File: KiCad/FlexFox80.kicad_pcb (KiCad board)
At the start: 4 copper layers, 111.2 x 80 mm, 315 parts, among them J101 Jumper_NO_Small, J102 Jumper_NO_Small, J203 V4, J307 Jumper_NC_Small, J501 GND, J502 DET, J503 DET, J504 GND, J505 DET, J506 GND, J507 DET, J508 GND, P101 Phoenix, P103 Phoenix, P202 To Power Supply Board, P203 AUX BATTERY, P301 ISP/PDI, P302 Thru, P303 Header, P304 Header, Q101 LMN400E01, Q102 IRF610, Q103 AFT05MS004N, U101 DAC081C085, U102 OPA171, U104 THS9001, U105 MIC5219-5.0YM5, U107 LM5134B, U110 MIC5219-3.3BM5, U201 DAC081C085, U202 OPA171, U203 LTC3600, U301 DS3231, U302 TS5A3157, U303 ATMEGA328P, U304 SI5351A, U305 74HC1G08, U306 MIC5219-3.3BM5, U307 SN74CB3Q3305, U308 MIC5219-3.3BM5, X301 ASTX-H11-25.MHZ

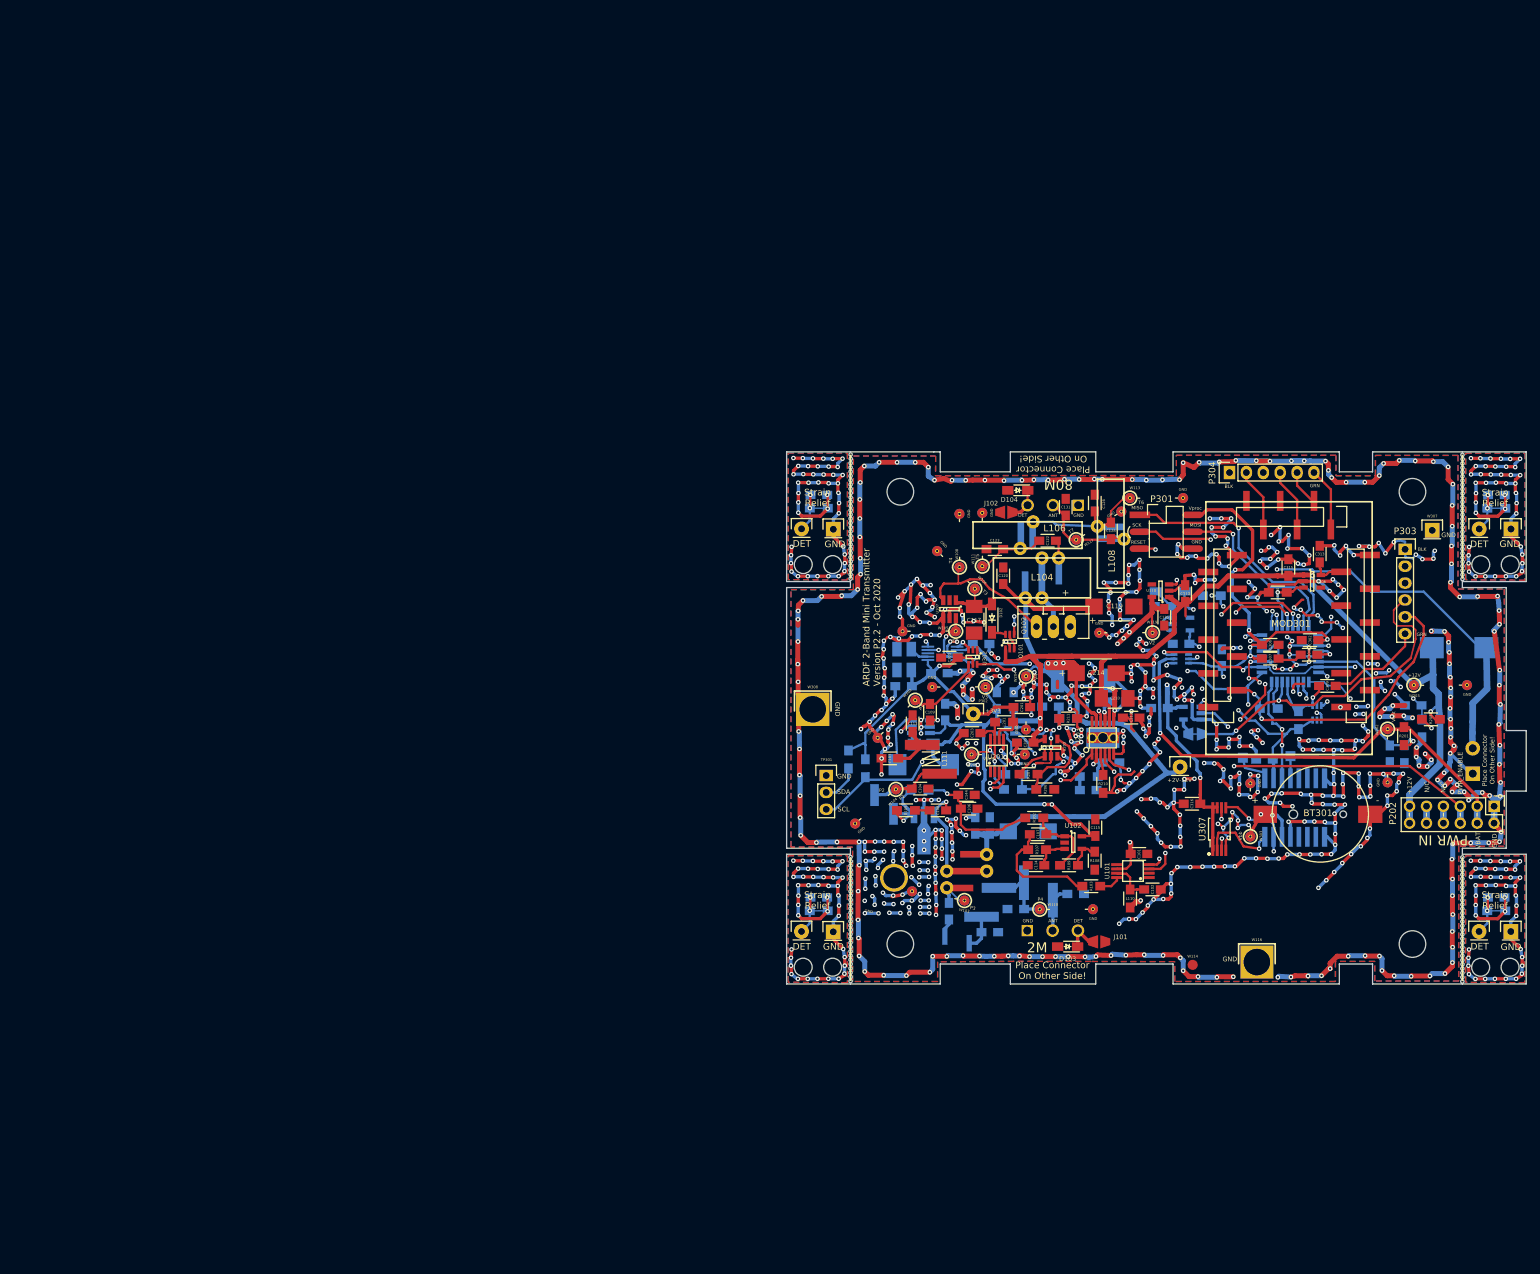
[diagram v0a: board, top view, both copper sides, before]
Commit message: PCB Updates
o Started PCB layout
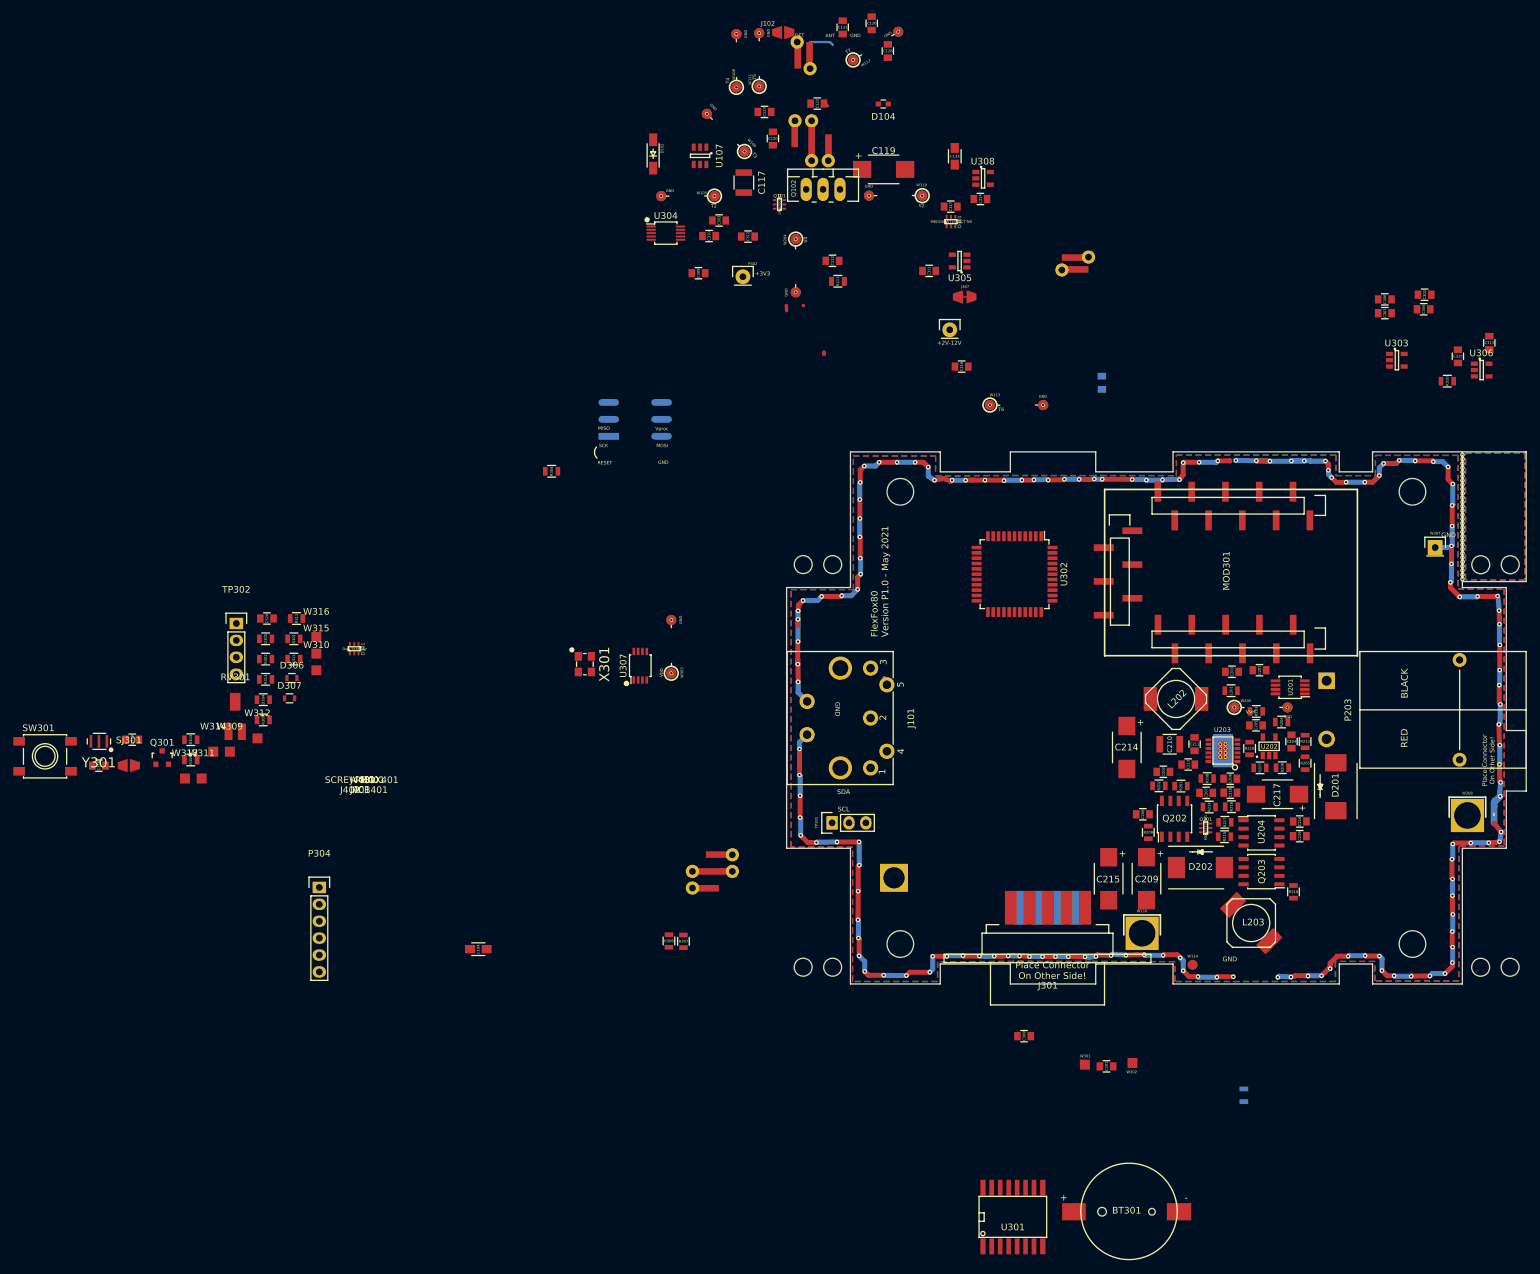
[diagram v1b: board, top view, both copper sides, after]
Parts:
- removed the ? at (117.8, 98.1)
- removed the ? at (117.8, 97.4)
- removed the ? at (117.8, 104.5)
- removed the ? at (117.8, 103.8)
- removed the ? at (117.8, 103.2)
- removed the ? at (117.8, 102.5)
- removed the ? at (117.8, 101.9)
- removed the ? at (117.8, 101.3)
- removed the ? at (117.8, 100.6)
- removed the ? at (117.8, 100.0)
- removed the ? at (117.8, 105.1)
- removed the ? at (117.8, 105.8)
- removed the ? at (117.8, 106.4)
- removed the ? at (117.8, 107.0)
- removed the ? at (117.8, 107.7)
- removed the ? at (117.8, 108.3)
- removed the ? at (117.8, 109.0)
- removed the ? at (117.8, 109.6)
- removed the ? at (117.8, 91.6)
- removed the ? at (117.8, 92.3)
- removed the ? at (117.8, 92.9)
- removed the ? at (117.8, 93.5)
- removed the ? at (117.8, 94.2)
- removed the ? at (117.8, 94.8)
- removed the ? at (117.8, 95.5)
- removed the ? at (117.8, 96.1)
- removed the ? at (117.8, 96.8)
- removed the ? at (117.8, 91.0)
- removed the ? at (25.8, 38.8)
- removed the ? at (25.8, 38.1)
- removed the ? at (25.8, 37.5)
- removed the ? at (25.8, 36.8)
- removed the ? at (25.8, 36.2)
- removed the ? at (25.8, 35.5)
- removed the ? at (25.8, 34.9)
- removed the ? at (25.8, 34.3)
- removed the ? at (25.8, 30.4)
- removed the ? at (25.8, 31.0)
- removed the ? at (25.8, 31.7)
- removed the ? at (25.8, 32.3)
- removed the ? at (25.8, 33.0)
- removed the ? at (25.8, 33.6)
- removed the ? at (25.8, 43.9)
- removed the ? at (25.8, 43.3)
- removed the ? at (25.8, 42.6)
- removed the ? at (25.8, 42.0)
- removed the ? at (25.8, 41.3)
- removed the ? at (25.8, 40.7)
- removed the ? at (25.8, 40.0)
- removed the ? at (25.8, 39.4)
- removed the ? at (25.8, 44.6)
- removed the ? at (25.8, 45.2)
- removed the ? at (25.8, 45.8)
- removed the ? at (25.8, 46.5)
- removed the ? at (25.8, 47.1)
- removed the ? at (25.8, 47.8)
- removed the ? at (25.8, 48.4)
- removed the ? at (25.8, 49.1)
- removed the ? at (25.8, 109.6)
- removed the ? at (25.8, 109.0)
- removed the ? at (25.8, 108.3)
- removed the ? at (25.8, 107.7)
- removed the ? at (25.8, 107.0)
- removed the ? at (25.8, 106.4)
- removed the ? at (25.8, 105.7)
- removed the ? at (25.8, 105.1)
- removed the ? at (25.8, 99.9)
- removed the ? at (25.8, 100.6)
- removed the ? at (25.8, 101.2)
- removed the ? at (25.8, 101.9)
- removed the ? at (25.8, 102.5)
- removed the ? at (25.8, 103.2)
- removed the ? at (25.8, 103.8)
- removed the ? at (25.8, 104.4)
- removed the ? at (25.8, 94.2)
- removed the ? at (25.8, 93.5)
- removed the ? at (25.8, 92.9)
- removed the ? at (25.8, 92.2)
- removed the ? at (25.8, 91.6)
- removed the ? at (25.8, 90.9)
- removed the ? at (25.8, 94.8)
- removed the ? at (25.8, 95.4)
- removed the ? at (25.8, 96.1)
- removed the ? at (25.8, 96.7)
- removed the ? at (25.8, 97.4)
- removed the ? at (25.8, 98.0)
- removed the ? at (25.8, 98.7)
- removed the ? at (25.8, 99.3)
- removed the ? at (117.8, 99.3)
- removed the ? at (117.8, 98.7)
- removed C101, C102: 10uF, Capacitors_SMD:C_0805_HandSoldering
- removed C103, C130: 20pF, Capacitors_SMD:C_0805_HandSoldering
- removed C105, C118: 100nF, Capacitors_SMD:C_0805_HandSoldering
- removed C106, C110: 10nF, Capacitors_SMD:C_0805_HandSoldering
- removed C107: 22nF, Capacitors_SMD:C_0805_HandSoldering
- removed C108, C109, C111, C113, C144: 1nF, Capacitors_SMD:C_0805_HandSoldering
- removed C112: 33pF, Capacitors_SMD:C_0805_HandSoldering
- removed C114: 33nF, Capacitors_SMD:C_0805_HandSoldering
- removed C115: 1uF, Capacitors_SMD:C_0805_HandSoldering
- removed C121: 100pF, Capacitors_SMD:C_0805_HandSoldering
- removed C125: 47uF low ESR, Capacitors_SMD:C_2917_7343_Metric_HandSoldering
- removed C132, C135, C141: 2.2uF, Capacitors_SMD:C_0805_HandSoldering
- removed C501, C502, C503, C504: np, Capacitors_SMD:C_0805_HandSoldering
- removed D103: 5V, Diodes_SMD:SOD-323F_Handsolder
- removed D302: 4.7V, Diodes_SMD:SOD-123_Handsolder
- removed D303: MBD54DWT1G_Schottky_Ind, TO_SOT_Packages_SMD:SOT-363_Handsolder
- removed J501, J504, J506, J508: GND, Pin_Headers:Pin_Header_Straight_1x01
- removed J502, J503, J505, J507: DET, Pin_Headers:Pin_Header_Straight_1x01_circle_pad
- removed L101: 82nH, Inductors:Wurth_744912212
- removed L102: 470nH, Inductors:L_0805_2015_Handsolder
- removed L105: 120nH, Inductors:Wurth_744912212
- removed L107: 8nH, Inductors:Wurth_744913080
- removed L109: 13nH, Inductors:Wurth_744911112
- removed L110: 10uH, Resistors_SMD:R_0805_HandSoldering
- removed L111: 56nH, Inductors:Wurth_744912212
- removed P101, P103: Phoenix, Sockets:Phoenix_3.81mm_3pos
- removed P202: To Power Supply Board, Pin_Headers:Pin_Header_Straight_2x06
- removed P303: Header, Pin_Headers:Pin_Header_Straight_1x06
- removed Q103: AFT05MS004N, TO_SOT_Packages_SMD:SOT89-3_Housing_Handsoldering
- removed R101: 49.9k, Resistors_SMD:R_0805_HandSoldering
- removed R102: 10, Resistors_SMD:R_0805_HandSoldering
- removed R103: 16k, Resistors_SMD:R_0805_HandSoldering
- removed R104: 51, Resistors_SMD:R_0805_HandSoldering
- removed R105: 270, Resistors_SMD:R_0805_HandSoldering
- removed R106: 240 2W, Resistors_SMD:R_2512_HandSoldering
- removed R107: 11k, Resistors_SMD:R_0805_HandSoldering
- removed R108: 15k, Resistors_SMD:R_0805_HandSoldering
- removed R109: 7.5k, Resistors_SMD:R_0805_HandSoldering
- removed R501, R502, R503, R504: 0, Resistors_SMD:Zero_Ohm_0805_HandSoldering
- removed U101: DAC081C085, SMD_Packages:SSOP-8_Handsolder
- removed U102: OPA171, TO_SOT_Packages_SMD:SOT-23-5_Handsolder
- removed U104: THS9001, TO_SOT_Packages_SMD:SOT-23-6_Handsolder
- removed U105: MIC5219-5.0YM5, TO_SOT_Packages_SMD:SOT-23-5_Handsolder
- removed U110: MIC5219-3.3BM5, TO_SOT_Packages_SMD:SOT-23-5_Handsolder
- removed W101: V3, Measurement_Points:Measurement_Point_ScopeProbe_Round-SMD-2sides-Pad_Small
- removed W102: P1, Measurement_Points:Measurement_Point_ScopeProbe_Round-SMD-2sides-Pad_Small
- removed W103: P3, Measurement_Points:Measurement_Point_ScopeProbe_Round-SMD-2sides-Pad_Small
- removed W104: P2, Measurement_Points:Measurement_Point_ScopeProbe_Round-SMD-2sides-Pad_Small
- removed W110: P4, Measurement_Points:Measurement_Point_ScopeProbe_Round-SMD-2sides-Pad_Small
- removed W202: Vbat, Measurement_Points:Measurement_Point_ScopeProbe_Round-SMD-2sides-Pad_Small
- removed W203: +12V, Measurement_Points:Measurement_Point_ScopeProbe_Round-SMD-2sides-Pad_Small
- added BOX401: Chassis Box, Oddities:Dummy_Empty, F.Cu at (-45.0, 81.8)
- added C206: 100nF, Capacitors_SMD:C_0805, F.Cu at (69.8, 84.5)
- added C209: 150uF low ESR, Capacitors_SMD:C_2917, F.Cu at (70.3, 94.2)
- added C215: 150uF low ESR, Capacitors_SMD:C_2917, F.Cu at (64.6, 94.2)
- added C216: 10uF, Capacitors_SMD:C_0805, F.Cu at (93.4, 85.6)
- added C217: 47uF low ESR, Capacitors_SMD:C_2917, F.Cu at (90.0, 81.5)
- added C218: 10nF, Capacitors_SMD:C_0805, F.Cu at (82.9, 81.2)
- added C219: 1uF, Capacitors_SMD:C_0805, F.Cu at (93.3, 87.8)
- added C318: 4.7uF, Capacitors_SMD:C_0805, F.Cu at (-87.2, 77.2)
- added C319: 100nF, Capacitors_SMD:C_0805, F.Cu at (-82.2, 73.3)
- added C320: 100nF, Capacitors_SMD:C_0805, F.Cu at (-61.9, 55.1)
- added D101: Dual Schottky, TO_SOT_Packages_SMD:SOT-363-0.65, F.Cu at (-48.8, 59.6)
- added D202: B530, Diodes_SMD:DO-214AB, F.Cu at (78.4, 92.5)
- added D304: GREEN, Resistors_SMD:R_0805, F.Cu at (-62.5, 67.3)
- added D305: RED, Resistors_SMD:R_0805, F.Cu at (-62.1, 58.1)
- added D306: ESD, Resistors_SMD:R_0603, F.Cu at (-58.2, 64.0)
- added D307: ESD, Resistors_SMD:R_0603, F.Cu at (-58.5, 67.1)
- added J301: DB9_Female, Connect:DB9F_CI, F.Cu at (55.5, 101.1)
- added J401: CONN_01X06, Oddities:Dummy_Empty, F.Cu at (-48.0, 83.3)
- added J402: CONN_01X10, Oddities:Dummy_Empty, F.Cu at (-49.5, 83.3)
- added J403: CONN_01X10, Oddities:Dummy_Empty, F.Cu at (-48.0, 81.8)
- added L203: 6.8uH, Inductors:CDR7D28MN, F.Cu at (86.0, 100.8)
- added PCB401: Circuit Board, Oddities:Dummy_Empty, F.Cu at (-46.5, 83.3)
- added PH401: Power Pole Staple, Oddities:Dummy_Empty, F.Cu at (-46.5, 81.8)
- added Q201: MUN5213DW1, TO_SOT_Packages_SMD:SOT-363-0.65, F.Cu at (79.2, 86.5)
- added Q202: DMP4025LSD, Housings_SOIC:SOIC-8_3.9x4.9mm_Pitch1.27mm, F.Cu at (74.5, 85.2)
- added Q203: RJK0354DSP, Housings_SOIC:SOIC-8_3.9x4.9mm_Pitch1.27mm, F.Cu at (87.6, 93.1)
- added Q301: PN2222A, TO_SOT_Packages_SMD:SOT-23, F.Cu at (-77.7, 76.0)
- added R209: 100k, Resistors_SMD:R_0805, F.Cu at (70.6, 87.2)
- added R214: 10k, Resistors_SMD:R_0805, F.Cu at (79.8, 83.4)
- added R215: 10k, Resistors_SMD:R_0805, F.Cu at (82.0, 87.9)
- added R216: 10k, Resistors_SMD:R_0805, F.Cu at (83.1, 83.3)
- added R217: 1.1k, Resistors_SMD:R_0805, F.Cu at (82.1, 85.7)
- added R218: 0.01 0.5W, Resistors_SMD:R_0805, F.Cu at (92.4, 96.2)
- added R301: 470, Resistors_SMD:R_0805, F.Cu at (-57.9, 58.1)
- added R302: 470, Resistors_SMD:R_0805, F.Cu at (-62.1, 61.2)
- added R303: 10k, Resistors_SMD:R_0805, F.Cu at (-73.4, 73.3)
- added R308: 100k, Resistors_SMD:R_0805, F.Cu at (-62.5, 70.3)
- added R309: 2.2k, Resistors_SMD:R_0805, F.Cu at (-73.4, 76.3)
- added R311: 10k, Resistors_SMD:R_0805, F.Cu at (-57.5, 55.1)
- added R312: 560k, Resistors_SMD:R_0805, F.Cu at (-57.9, 61.2)
- added R313: 100k, Resistors_SMD:R_0805, F.Cu at (-62.1, 64.2)
- added RV301: 10k Pot, Potentiometers:Potentiometer_ST32ET_Handsolder, F.Cu at (-66.7, 69.8)
- added SCREW401: QTY 4 SCREWS, Oddities:Dummy_Empty, F.Cu at (-49.5, 81.8)
- added SJ301: SolderJumper_2_Open, Wire_Connections_Bridges:Solder-Jumper-NO-SMD-Pad_Small, F.Cu at (-82.7, 77.2)
- added SW301: SPST, Buttons_Switches_SMD:PTS645SL50SMTR92, F.Cu at (-95.3, 75.8)
- added TP302: I2C0, Pin_Headers:Pin_Header_Straight_1x04, F.Cu at (-66.5, 55.8)
- added U204: MIC2196, Housings_SOIC:SOIC-8_3.9x4.9mm_Pitch1.27mm, F.Cu at (87.6, 87.3)
- added W309: TEST_1P, Measurement_Points:Measurement_Point_Square-SMD-Pad_Small, F.Cu at (-67.5, 75.1)
- added W310: TEST_1P, Measurement_Points:Measurement_Point_Square-SMD-Pad_Small, F.Cu at (-54.5, 62.8)
- added W311: TEST_1P, Measurement_Points:Measurement_Point_Square-SMD-Pad_Small, F.Cu at (-71.8, 79.1)
- added W312: TEST_1P, Measurement_Points:Measurement_Point_Square-SMD-Pad_Small, F.Cu at (-63.4, 73.1)
- added W313: TEST_1P, Measurement_Points:Measurement_Point_Square-SMD-Pad_Small, F.Cu at (-74.3, 79.1)
- added W314: TEST_1P, Measurement_Points:Measurement_Point_Square-SMD-Pad_Small, F.Cu at (-70.0, 75.1)
- added W315: TEST_1P, Measurement_Points:Measurement_Point_Square-SMD-Pad_Small, F.Cu at (-54.5, 60.3)
- added W316: TEST_1P, Measurement_Points:Measurement_Point_Square-SMD-Pad_Small, F.Cu at (-54.5, 57.8)
- added Y301: 20 MHz, Crystals:CSTNE20M0V53Z000R0, F.Cu at (-87.2, 73.5)
- C117, C210: footprint Capacitors_SMD:C_1210_HandSoldering -> Capacitors_SMD:C_1210
- C119, C214: footprint Capacitors_SMD:C_2917_7343_Metric_HandSoldering -> Capacitors_SMD:C_2917
- C120, C122, C123, C126, C128, C131, C201, C203, C205, C213, C302, C304, C305, C306, C307, C309, C316: footprint Capacitors_SMD:C_0805_HandSoldering -> Capacitors_SMD:C_0805
- C202, C204, C207, C208, C211, C212, C301, C308, C310, C311, C312: footprint Capacitors_SMD:C_0805_HandSoldering -> Capacitors_SMD:C_0805; moved to F.Cu
- C303: value 100nF -> 4.7uF; footprint Capacitors_SMD:C_0805_HandSoldering -> Capacitors_SMD:C_0805
- C313, C315: value 2.2uF -> 4.7uF; footprint Capacitors_SMD:C_0805_HandSoldering -> Capacitors_SMD:C_0805
- C314, C317: value 2.2uF -> 4.7uF; footprint Capacitors_SMD:C_0805_HandSoldering -> Capacitors_SMD:C_0805; moved to F.Cu
- D104: footprint Diodes_SMD:SOD-323F_Handsolder -> Capacitors_SMD:C_0603
- D201: footprint Diodes_SMD:DO-214AB_Handsoldering -> Diodes_SMD:DO-214AB; moved to F.Cu
- D301: value D_Schottky_x2_KCom_Dual -> MBD54DWT1GOSCT-ND; footprint TO_SOT_Packages_SMD:SOT-363_Handsolder -> TO_SOT_Packages_SMD:SOT-363-0.65; moved to F.Cu
- J101: value Jumper_NO_Small -> DIN-5_180degree; footprint Wire_Connections_Bridges:Solder-Jumper-NO-SMD-Pad_Small -> Connect:SDF-50J
- J307, L202, W301, W302: moved to F.Cu
- L104, L106, L108, P301: moved to B.Cu
- L201, R201, R205, R206, R207, R210, R212, R305, R310: footprint Resistors_SMD:R_0805_HandSoldering -> Resistors_SMD:R_0805
- P203: value AUX BATTERY -> Power Pole; footprint Sockets:Phoenix_3.81mm_2pos -> Connect:PowerPole-ASMPP30-1x2; moved to F.Cu
- Q101: value LMN400E01 -> LMN200B02; footprint TO_SOT_Packages_SMD:SOT-363_Handsolder -> TO_SOT_Packages_SMD:SOT-363-0.65
- R202, R203, R204, R208, R304, R306, R307: footprint Resistors_SMD:R_0805_HandSoldering -> Resistors_SMD:R_0805; moved to F.Cu
- R211: value 12.4k -> 10k; footprint Resistors_SMD:R_0805_HandSoldering -> Resistors_SMD:R_0805
- R213: value 12.4k -> 10k; footprint Resistors_SMD:R_0805_HandSoldering -> Resistors_SMD:R_0805; moved to F.Cu
- TP301: value I2C -> I2C1
- U107: footprint TO_SOT_Packages_SMD:SOT-23-6_Handsolder -> TO_SOT_Packages_SMD:SOT-23-6-LM5134
- U201: footprint SMD_Packages:SSOP-8_Handsolder -> Housings_SSOP:MSOP-8_3x3mm_Pitch0.65mm
- U202: footprint TO_SOT_Packages_SMD:SOT-23-5_Handsolder -> TO_SOT_Packages_SMD:SOT-23-5_MCP
- U203: footprint SMD_Packages:SSOP-12_Pad_Handsolder -> Housings_SSOP:SSOP-12_Pad
- U301: footprint SMD_Packages:SO16_Handsolder -> SMD_Packages:SO16; moved to F.Cu
- U302: value TS5A3157 -> ATmega1284P-AU; footprint TO_SOT_Packages_SMD:SOT-363_Handsolder -> Housings_QFP:TQFP-44_10x10mm_Pitch0.8mm
- U303: value ATMEGA328P -> LP2992; footprint Housings_QFP:TQFP-32_7x7mm_Pitch0.8mm -> TO_SOT_Packages_SMD:SOT-23-5; moved to F.Cu
- U304: footprint Housings_SSOP:MSOP-10_3x3mm_Pitch0.5mm_Handsolder -> Housings_SSOP:MSOP-10_3x3mm_Pitch0.5mm; moved to F.Cu
- U305: footprint TO_SOT_Packages_SMD:SOT-23-5_Handsolder -> TO_SOT_Packages_SMD:SOT-23-5; moved to F.Cu
- U306: value MIC5219-3.3BM5 -> LP2992; footprint TO_SOT_Packages_SMD:SOT-23-5_Handsolder -> TO_SOT_Packages_SMD:SOT-23-5
- U307: footprint Housings_SSOP:TSSOP-8_3x3mm_Pitch0.65mm_Handsolder -> Housings_SSOP:TSSOP-8_3x3mm_Pitch0.65mm
- U308: value MIC5219-3.3BM5 -> LP2992; footprint TO_SOT_Packages_SMD:SOT-23-5_Handsolder -> TO_SOT_Packages_SMD:SOT-23-5; moved to F.Cu
- X301: footprint Crystals:ASTX-H11 -> Crystals:ASTX-H11-25.000MHZ; moved to F.Cu
- moved P304 150.4 mm to (-54.1, 95.5), turned to 0 degrees
- moved R304 113.6 mm to (-19.1, 32.9)
- moved W308 99.7 mm to (118.6, 84.7)
- moved U307 90.5 mm to (-5.80, 62.1)
- moved W303 90.5 mm to (-1.14, 63.3)
- moved D102 86.4 mm to (-3.87, -14.8)
- moved P301 80.7 mm to (-7.84, 27.6)
- moved C131 79.6 mm to (24.6, -33.8)
- moved W117 79.6 mm to (26.2, -28.9)
- moved C126 79.6 mm to (29.0, -34.4)
- moved C128 79.6 mm to (31.4, -30.3)
- moved J102 79.6 mm to (15.7, -33.1)
- moved L106 79.6 mm to (18.9, -29.6), turned to 270 degrees
- moved W108 79.6 mm to (8.65, -24.8)
- moved W111 79.6 mm to (12.1, -25.0)
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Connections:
- C123 pad 1: Net-(C122-Pad1) -> Net-(C122-Pad2)
- C202 pad 1: TX_BATTERY_VOLTAGE -> TX_+12_VOLTAGE
- C204 pad 1: TX_+12_VOLTAGE -> GND
- C204 pad 2: GND -> TX_BATTERY_VOLTAGE
- C212 pad 1: TX_PA_VOLTAGE -> GND
- C212 pad 2: GND -> TX_PA_VOLTAGE
- C302 pad 1: Vproc -> GND
- C302 pad 2: GND -> Vproc
- C303 pad 1: +3V3_L8 -> GND
- C303 pad 2: GND -> +12V
- C306 pad 1: Vproc -> GND
- C306 pad 2: GND -> Vproc
- C312 pad 1: GND -> +3V3_L8
- C312 pad 2: +3V3_L8 -> GND
- C314 pad 2: Net-(C314-Pad2) -> EXTERNAL_3.2V-12V_SUPPLY
- C316 pad 1: +3V3_L8 -> GND
- C316 pad 2: GND -> +3V3_L8
- C317 pad 2: Net-(C317-Pad2) -> Vproc
- D201 pad 1: +12V -> EXTERNAL_3.2V-12V_SUPPLY
- D201 pad 2: AUX_BAT_DIRECT -> Net-(D201-Pad2)
- D301 pad 1: Net-(C317-Pad2) -> Net-(D301-Pad1)
- D301 pad 2: VBAT_UNINTERRUPTED -> Net-(D301-Pad2)
- D301 pad 3: 80M_ANTENNA_DETECT -> Vproc
- D301 pad 4: Net-(D301-Pad4) -> ~RESET~
- D301 pad 5: ~ANT_CONNECT_INT~ -> Net-(D301-Pad5)
- J101 pad 1: GND -> Net-(J101-Pad1)
- J101 pad 2: 2M_ANTENNA_DETECT -> GND
- L104 pad 3: Net-(C122-Pad2) -> Net-(C122-Pad1)
- L106 pad 1: Net-(C122-Pad1) -> Net-(C122-Pad2)
- L202 pad 1: Net-(C211-Pad2) -> Net-(C211-Pad1)
- P203 pad 2: AUX_BAT_DIRECT -> Net-(D201-Pad2)
- R201 pad 1: VBAT_UNINTERRUPTED -> TX_+12_VOLTAGE
- R201 pad 2: TX_BATTERY_VOLTAGE -> +12V
- R202 pad 1: TX_BATTERY_VOLTAGE -> TX_+12_VOLTAGE
- R205 pad 1: +12V -> Net-(D201-Pad2)
- R205 pad 2: TX_+12_VOLTAGE -> TX_BATTERY_VOLTAGE
- R208 pad 1: Net-(C207-Pad1) -> Net-(C208-Pad1)
- R208 pad 2: Net-(C208-Pad1) -> Net-(C207-Pad1)
- R211 pad 1: GND -> TX_PA_VOLTAGE
- R211 pad 2: TX_PA_VOLTAGE -> GND
- R213 pad 1: TX_+12_VOLTAGE -> TX_BATTERY_VOLTAGE
- R304 pad 1: /Digital/PD1 -> /Digital/TXD0
- R304 pad 2: DI_TXD0 -> TXD_TO_FTDI
- R305 pad 1: Vproc -> ~RESET~
- R305 pad 2: ~RESET~ -> Vproc
- U203 pad 7: Net-(C211-Pad2) -> Net-(C211-Pad1)
- U203 pad 9: Net-(C211-Pad1) -> Net-(C211-Pad2)
- U302 pad 1: CLK0 -> MOSI
- U302 pad 2: GND -> MISO
- U302 pad 3: CLK2 -> SCK
- U302 pad 4: VHF_CLK -> ~RESET~
- U302 pad 5: +3V3_L8 -> Vproc
- U302 pad 6: VHF_CLK_SEL -> GND
- U303 pad 1: ~ANT_CONNECT_INT~ -> +12V
- U303 pad 2: 80M_ANTENNA_DETECT -> GND
- U303 pad 3: GND -> 3V3_PWR_ENABLE
- U303 pad 4: Vproc -> Net-(U303-Pad4)
- U303 pad 5: GND -> +3V3_L8
- U304 pad 10: CLK0 -> Net-(U304-Pad10)
- U304 pad 6: CLK2 -> Net-(U304-Pad6)
- U305 pad 4: Net-(J307-Pad2) -> /Digital/RXD1
- U308 pad 1: Net-(C314-Pad2) -> EXTERNAL_3.2V-12V_SUPPLY
- U308 pad 3: Net-(C314-Pad2) -> EXTERNAL_3.2V-12V_SUPPLY
- U308 pad 5: Net-(C317-Pad2) -> Vproc
- W111 pad 1: Net-(C122-Pad1) -> Net-(C122-Pad2)
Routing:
- net GND: track 1398.8 -> 386.4 mm, vias 684 -> 139
- net +3V3_L8: track 208.3 -> 0.00 mm, vias 9 -> 0
- net +12V: track 157.2 -> 0.06 mm, vias 4 -> 0
- net +2to+12V: track 134.8 -> 0.00 mm, vias 3 -> 0
- net DI_SDA: track 110.6 -> 0.00 mm, vias 4 -> 0
- net 2M_ANTENNA_DETECT: track 105.8 -> 0.00 mm, vias 3 -> 0
- net 80M_ANTENNA_DETECT: track 105.3 -> 1.47 mm, vias 3 -> 0
- net DI_SCL: track 100.1 -> 0.00 mm, vias 5 -> 0
- net Vproc: track 93.6 -> 0.00 mm, vias 7 -> 0
- net VHF_ENABLE: track 73.9 -> 0.00 mm, vias 3 -> 0
- net VBAT_UNINTERRUPTED: track 72.8 -> 0.00 mm, vias 1 -> 0
- net AUX_BAT_DIRECT: track 71.5 -> 0.00 mm, vias 2 -> 0
- net GND_L2: track 70.1 -> 0.00 mm, vias 43 -> 0
- net GND_L3: track 70.1 -> 0.00 mm, vias 43 -> 0
- net GND_L0: track 70.1 -> 0.00 mm, vias 43 -> 0
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- removed copper zone on B.Cu, net GND_L1
- removed copper zone on F.Cu, net GND_L1
- removed copper zone on In1.Cu, net GND_L1
- removed copper zone on In2.Cu, net GND_L1
- removed copper zone on B.Cu, net GND_L2
- removed copper zone on F.Cu, net GND_L2
- removed copper zone on In1.Cu, net GND_L2
- removed copper zone on In2.Cu, net GND_L2
- removed copper zone on B.Cu, net GND_L3
- removed copper zone on F.Cu, net GND_L3
- removed copper zone on In1.Cu, net GND_L3
- removed copper zone on In2.Cu, net GND_L3
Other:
- outline, holes or cut-outs redrawn
- board text added: "FlexFox80 Version P1.0 - May 2021"
- board text removed: "+12V"
- board text removed: "+12VPS"
- board text removed: "2M"
- board text removed: "80M"
- board text removed: "ARDF 2-Band Mini Transmitter Version P2.2 - Oct 2020"
- board text removed: "AUX PWR"
- board text removed: "BLK"
- board text removed: "GRN"
- board text removed: "N/C"
- board text removed: "P1"
- board text removed: "P2"
- board text removed: "P3"
- board text removed: "P4"
- board text removed: "PWR IN"
- board text removed: "PWR_ENABLE"
- board text removed: "Strain Relief"
- board text removed: "T3"
- board text removed: "T4"
- board text removed: "T6"
- board text removed: "T7"
- board text removed: "TP301"
- board text removed: "V3"
- board text removed: "VBAT"
- board text removed: "Vbat"

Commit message: PCB Updates
Layout work
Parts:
- removed the 4mm thru at (32.4, 94.0)
- removed the ? at (23.1, 107.5)
- removed the ? at (117.8, 48.5)
- removed the ? at (117.8, 47.8)
- removed the ? at (117.8, 47.2)
- removed the ? at (18.7, 107.5)
- removed the ? at (117.8, 43.3)
- removed the ? at (18.7, 47.0)
- removed the ? at (117.8, 35.0)
- removed the ? at (117.8, 38.8)
- removed the ? at (23.1, 47.0)
- removed the ? at (120.6, 47.0)
- removed the ? at (125.0, 47.0)
- removed the ? at (120.5, 107.5)
- removed the ? at (125.0, 107.5)
- removed the ? at (117.8, 49.1)
- removed BOX401: Chassis Box, Oddities:Dummy_Empty
- removed C104: 68pF, Capacitors_SMD:C_0805_HandSoldering
- removed C133: 2.2uF, Capacitors_SMD:C_0805_HandSoldering
- removed J102: Jumper_NO_Small, Wire_Connections_Bridges:Solder-Jumper-NO-SMD-Pad_Small
- removed J307: Jumper_NC_Small, Wire_Connections_Bridges:Solder-Jumper-NC-SMD-Pad_Small
- removed J401: CONN_01X06, Oddities:Dummy_Empty
- removed J402, J403: CONN_01X10, Oddities:Dummy_Empty
- removed L103: 7T #24 Bifilar T50-0, Inductors:Toroid_T-50A_TH_BF_CT_Vertical
- removed PCB401: Circuit Board, Oddities:Dummy_Empty
- removed PH401: Power Pole Staple, Oddities:Dummy_Empty
- removed SCREW401: QTY 4 SCREWS, Oddities:Dummy_Empty
- removed W114: GND, Measurement_Points:Measurement_Point_Round-SMD-Pad_Small
- removed W117: T7, Measurement_Points:Measurement_Point_ScopeProbe_Round-SMD-2sides-Pad_Small
- removed W119: V2, Measurement_Points:Measurement_Point_ScopeProbe_Round-SMD-2sides-Pad_Small
- removed W301, W302, W309, W310, W311, W312, W313, W314, W315, W316: TEST_1P, Measurement_Points:Measurement_Point_Square-SMD-Pad_Small
- removed W303: Vbb, Measurement_Points:Measurement_Point_ScopeProbe_Round-SMD-2sides-Pad_Small
- added J302: Conn_01x06, Pin_Headers:Pin_Header_Angled_1x06, B.Cu at (119.8, 32.4)
- added J303: DB9_Male, Connect:DB9F_CI, F.Cu at (127.2, 38.7)
- BT301, P203: moved to B.Cu
- C305, R212, R305: moved to F.Cu
- moved D305 186.3 mm to (108.3, 133.3)
- moved D304 183.1 mm to (110.5, 127.3)
- moved P304 179.3 mm to (104.9, 12.5)
- moved R301 177.5 mm to (104.1, 130.7)
- moved R302 173.0 mm to (94.5, 134.4)
- moved Y301 172.7 mm to (78.5, 122.0)
- moved R304 156.6 mm to (109.2, 122.6)
- moved U308 149.2 mm to (96.8, 129.0)
- moved C314 145.1 mm to (103.4, 125.0)
- moved C317 141.6 mm to (98.0, 122.7)
- moved C319 139.1 mm to (46.8, 125.1)
- moved SW301 130.1 mm to (33.5, 94.7)
- moved SJ301 130.1 mm to (34.3, 134.0)
- moved D301 128.6 mm to (35.9, 123.8)
- moved RV301 123.3 mm to (40.5, 130.7)
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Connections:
- net EXTERNAL_3.2V-12V_SUPPLY renamed EXTERNAL_3.6V-15V_SUPPLY
- D301 pad 2: Net-(D301-Pad2) -> (no net)
- D301 pad 5: Net-(D301-Pad5) -> (no net)
- J101 pad 1: Net-(J101-Pad1) -> (no net)
- J101 pad 4: Net-(J101-Pad4) -> (no net)
- J301 pad 4: Net-(J301-Pad4) -> (no net)
- MOD301 pad 12: Net-(MOD301-Pad12) -> (no net)
- MOD301 pad 13: Net-(MOD301-Pad13) -> (no net)
- MOD301 pad 15: Net-(MOD301-Pad15) -> (no net)
- MOD301 pad 23: Net-(MOD301-Pad23) -> (no net)
- MOD301 pad 3: Net-(MOD301-Pad3) -> (no net)
- MOD301 pad 5: Net-(MOD301-Pad5) -> (no net)
- MOD301 pad 8: Net-(MOD301-Pad8) -> (no net)
- P304 pad 3: Net-(P304-Pad3) -> (no net)
- U107 pad 2: Net-(U107-Pad2) -> (no net)
- U201 pad 1: Net-(U201-Pad1) -> (no net)
- U201 pad 2: Net-(U201-Pad2) -> (no net)
- U203 pad 12: Net-(U203-Pad12) -> (no net)
- U302 pad 36: /Digital/PA1 -> (no net)
- U302 pad 37: /Digital/PA0 -> (no net)
- U302 pad 41: /Digital/PB1 -> (no net)
- U302 pad 44: /Digital/PB4 -> (no net)
- U303 pad 4: Net-(U303-Pad4) -> (no net)
- U304 pad 10: Net-(U304-Pad10) -> (no net)
- U304 pad 3: Net-(U304-Pad3) -> (no net)
- U304 pad 6: Net-(U304-Pad6) -> (no net)
- U306 pad 4: Net-(U306-Pad4) -> (no net)
- U308 pad 4: Net-(U308-Pad4) -> (no net)
- X301 pad 1: Net-(X301-Pad1) -> (no net)
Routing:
- net GND1: track 0.00 -> 29.9 mm, vias 0 -> 8
- net Net-(R207-Pad1): track 0.00 -> 27.6 mm, vias 0 -> 1
- net +12V: track 0.06 -> 23.9 mm
- net +2to+12V: track 0.00 -> 23.9 mm, vias 0 -> 4
- net Net-(C213-Pad1): track 0.00 -> 23.2 mm, vias 0 -> 2
- net Net-(C211-Pad1): track 0.00 -> 15.9 mm
- net Net-(C211-Pad2): track 0.00 -> 15.1 mm
- net Net-(J302-Pad6): track 0.00 -> 13.7 mm
- net GND: track 386.4 -> 394.5 mm, vias 139 -> 146
- net Net-(C208-Pad1): track 0.00 -> 6.24 mm
- net Net-(J302-Pad5): track 0.00 -> 5.01 mm
- net Net-(J302-Pad3): track 0.00 -> 4.93 mm
- net Net-(J302-Pad4): track 0.00 -> 4.90 mm
- net Net-(R210-Pad1): track 0.00 -> 4.44 mm
- net Net-(C209-Pad1): track 0.00 -> 3.75 mm
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- added copper zone on B.Cu, net GND1
- added copper zone on F.Cu, net GND1
- added copper zone on In1.Cu, net GND1
- added copper zone on In2.Cu, net GND1
- removed copper zone on B.Cu, net GND_L0
- removed copper zone on F.Cu, net GND_L0
- removed copper zone on In1.Cu, net GND_L0
- removed copper zone on In2.Cu, net GND_L0
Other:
- outline, holes or cut-outs redrawn
- board text removed: "+2V-12V"
- board text removed: "+3V3"
- board text removed: "ANT"
- board text removed: "Back of U203"
- board text removed: "DET"
- board text removed: "T2"
- board text removed: "T5"
- board text removed: "V2"
- board text removed: "V4"
- board text removed: "V5"
- board text removed: "Vbb"
